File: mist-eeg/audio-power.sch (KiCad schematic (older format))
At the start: 18 parts, among them U6 LT3042xMSE, U7 LT3042xMSE

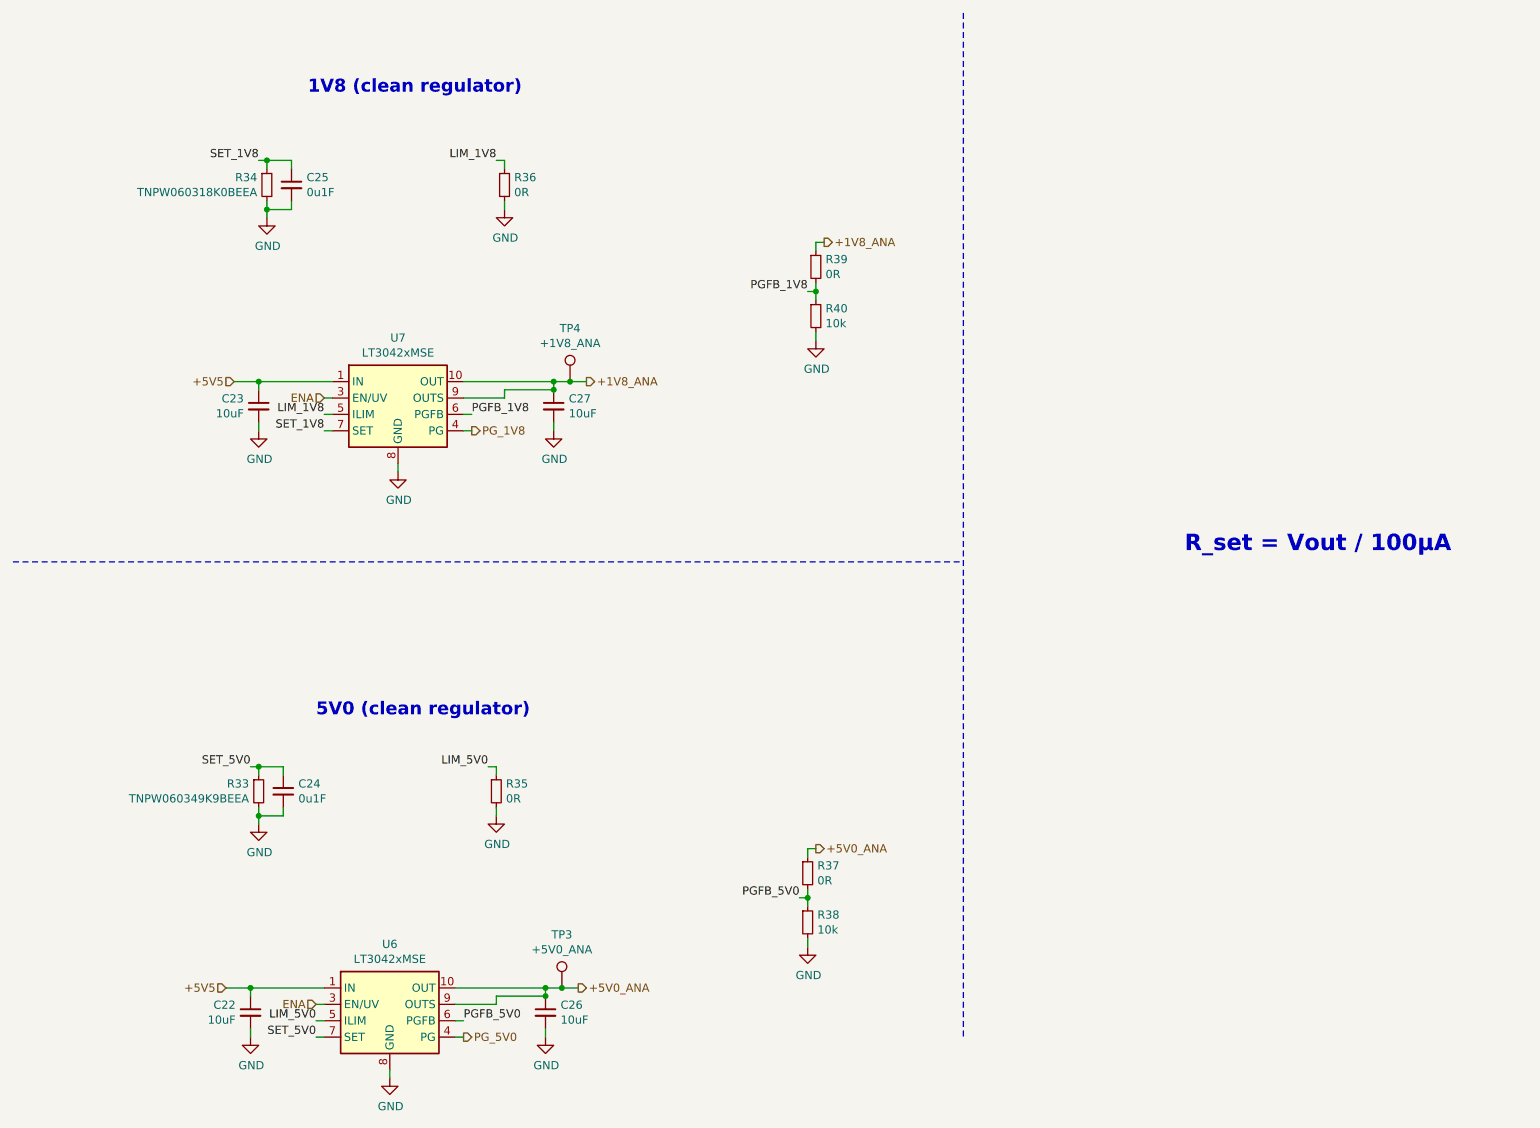
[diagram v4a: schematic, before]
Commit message: Change buckboost regulator used
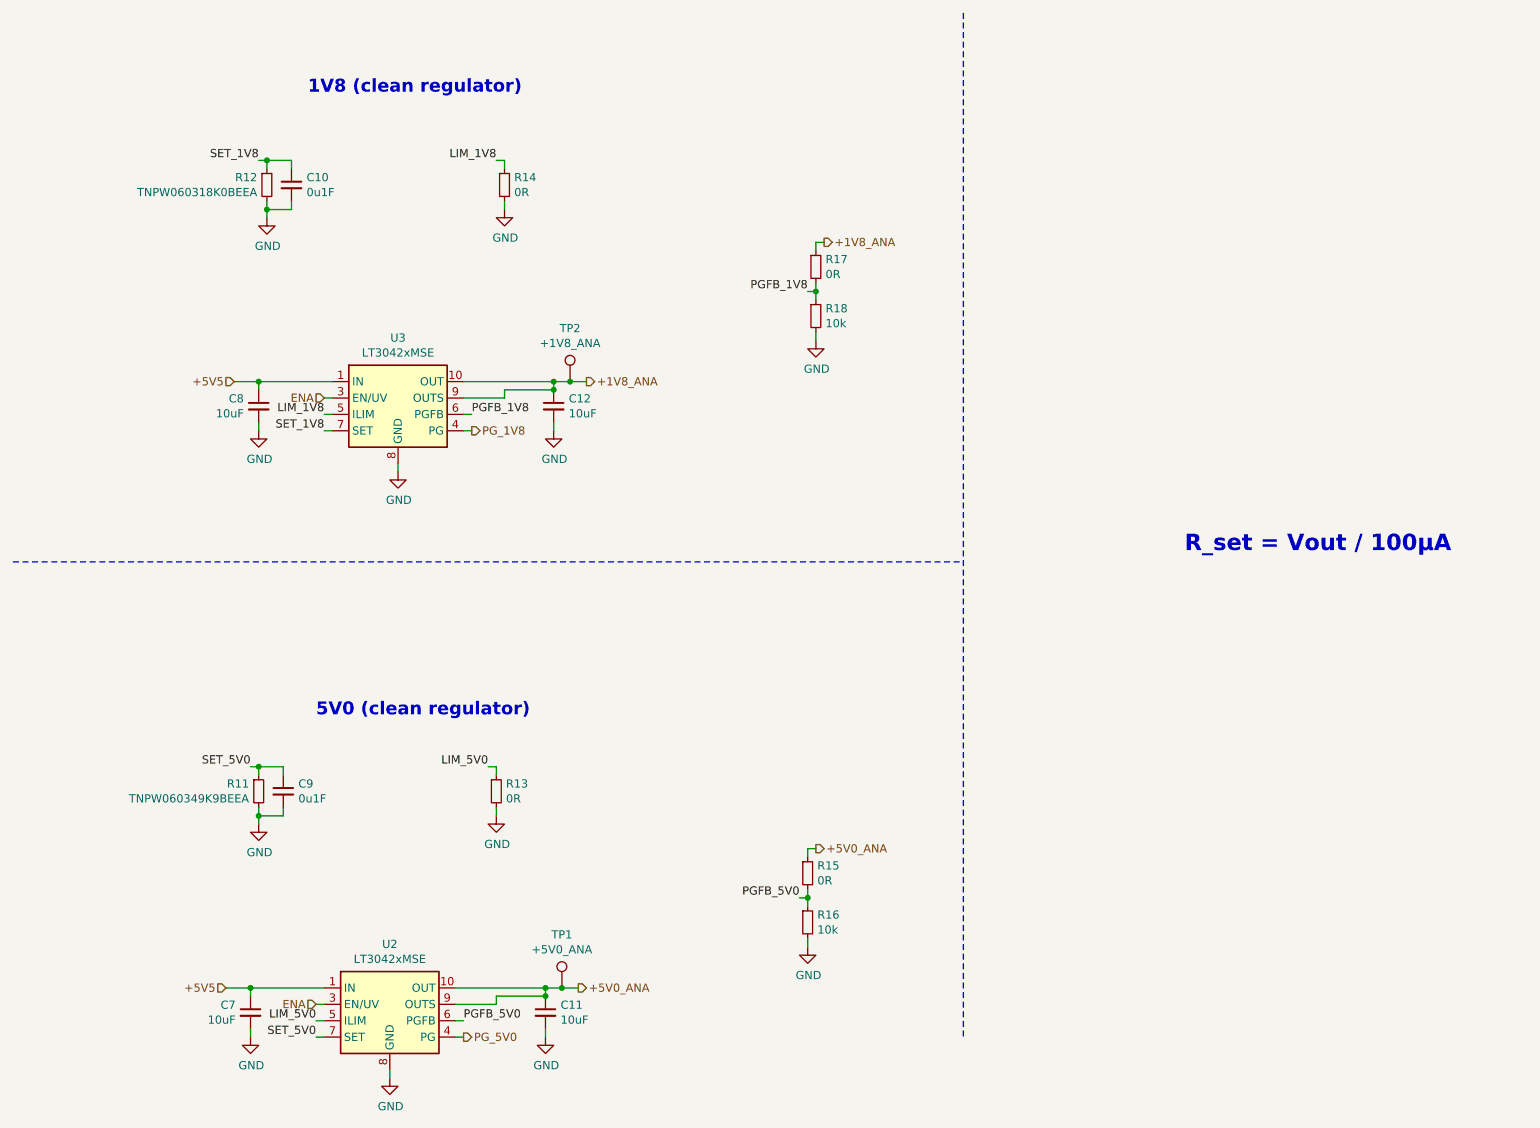
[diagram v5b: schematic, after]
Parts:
- renumbered C25 to C10, C26 to C11, C27 to C12, C22 to C7, C23 to C8, C24 to C9, R33 to R11, R34 to R12, R35 to R13, R36 to R14, R37 to R15, R38 to R16, R39 to R17, R40 to R18, TP3 to TP1, TP4 to TP2, U6 to U2, U7 to U3
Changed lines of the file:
@@
 Sheet 4 11
 Title "Portiloop"
-Date "2021-06-07"
-Rev "1A"
+Date "2021-08-03"
+Rev "1D"
 Comp "MIST Lab"
 Comment1 "Designed by Xavier L'Heureux"
@@
 $EndDescr
 $Comp
-L Regulator_Linear:LT3042xMSE U7
+L Regulator_Linear:LT3042xMSE U3
 U 1 1 60CC3292
 P 2850 2850
-F 0 "U7" H 2850 3217 50  0000 C CNN
+F 0 "U3" H 2850 3217 50  0000 C CNN
 F 1 "LT3042xMSE" H 2850 3126 50  0000 C CNN
 F 2 "Package_SO:MSOP-10-1EP_3x3mm_P0.5mm_EP1.68x1.88mm" H 2850 3175 50  0001 C CNN
@@
 +5V0_ANA
 $Comp
-L Device:C_Small C23
+L Device:C_Small C8
 U 1 1 60CDC893
 P 2000 2900
-F 0 "C23" H 1909 2946 50  0000 R CNN
+F 0 "C8" H 1909 2946 50  0000 R CNN
 F 1 "10uF" H 1909 2855 50  0000 R CNN
 F 2 "Capacitor_SMD:C_0603_1608Metric" H 2000 2900 50  0001 C CNN
@@
 	2000 3000 2000 3050
 $Comp
-L Device:C_Small C27
+L Device:C_Small C12
 U 1 1 60CE9660
 P 3800 2900
-F 0 "C27" H 3892 2946 50  0000 L CNN
+F 0 "C12" H 3892 2946 50  0000 L CNN
 F 1 "10uF" H 3892 2855 50  0000 L CNN
 F 2 "Capacitor_SMD:C_0603_1608Metric" H 3800 2900 50  0001 C CNN
@@
 	2400 2950 2450 2950
 $Comp
-L Device:R_Small R36
+L Device:R_Small R14
 U 1 1 60CFCD89
 P 3500 1550
-F 0 "R36" H 3559 1596 50  0000 L CNN
+F 0 "R14" H 3559 1596 50  0000 L CNN
 F 1 "0R" H 3559 1505 50  0000 L CNN
 F 2 "Resistor_SMD:R_0603_1608Metric" H 3500 1550 50  0001 C CNN
@@
 $EndComp
 $Comp
-L Device:R_Small R39
+L Device:R_Small R17
 U 1 1 60D00084
 P 5400 2050
-F 0 "R39" H 5459 2096 50  0000 L CNN
+F 0 "R17" H 5459 2096 50  0000 L CNN
 F 1 "0R" H 5459 2005 50  0000 L CNN
 F 2 "Resistor_SMD:R_0603_1608Metric" H 5400 2050 50  0001 C CNN
@@
 $EndComp
 $Comp
-L Device:R_Small R40
+L Device:R_Small R18
 U 1 1 60D0018E
 P 5400 2350
-F 0 "R40" H 5459 2396 50  0000 L CNN
+F 0 "R18" H 5459 2396 50  0000 L CNN
 F 1 "10k" H 5459 2305 50  0000 L CNN
 F 2 "Resistor_SMD:R_0603_1608Metric" H 5400 2350 50  0001 C CNN
@@
 	3500 1700 3500 1650
 $Comp
-L Device:R_Small R34
+L Device:R_Small R12
 U 1 1 60D04DA7
 P 2050 1550
-F 0 "R34" H 1991 1596 50  0000 R CNN
+F 0 "R12" H 1991 1596 50  0000 R CNN
 F 1 "TNPW060318K0BEEA" H 1991 1505 50  0000 R CNN
 F 2 "Resistor_SMD:R_0603_1608Metric" H 2050 1550 50  0001 C CNN
@@
 	5400 2200 5400 2250
 $Comp
-L Device:C_Small C25
+L Device:C_Small C10
 U 1 1 60D11AAE
 P 2200 1550
-F 0 "C25" H 2292 1596 50  0000 L CNN
+F 0 "C10" H 2292 1596 50  0000 L CNN
 F 1 "0u1F" H 2292 1505 50  0000 L CNN
 F 2 "Capacitor_SMD:C_0201_0603Metric" H 2200 1550 50  0001 C CNN
@@
 R_set = Vout / 100μA
 $Comp
-L Regulator_Linear:LT3042xMSE U6
+L Regulator_Linear:LT3042xMSE U2
 U 1 1 60D644F1
 P 2800 6550
-F 0 "U6" H 2800 6917 50  0000 C CNN
+F 0 "U2" H 2800 6917 50  0000 C CNN
 F 1 "LT3042xMSE" H 2800 6826 50  0000 C CNN
 F 2 "Package_SO:MSOP-10-1EP_3x3mm_P0.5mm_EP1.68x1.88mm" H 2800 6875 50  0001 C CNN
@@
 +5V0_ANA
 $Comp
-L Device:C_Small C22
+L Device:C_Small C7
 U 1 1 60D644F9
 P 1950 6600
-F 0 "C22" H 1859 6646 50  0000 R CNN
+F 0 "C7" H 1859 6646 50  0000 R CNN
 F 1 "10uF" H 1859 6555 50  0000 R CNN
 F 2 "Capacitor_SMD:C_0603_1608Metric" H 1950 6600 50  0001 C CNN
@@
 	1950 6700 1950 6750
 $Comp
-L Device:C_Small C26
+L Device:C_Small C11
 U 1 1 60D6450F
 P 3750 6600
-F 0 "C26" H 3842 6646 50  0000 L CNN
+F 0 "C11" H 3842 6646 50  0000 L CNN
 F 1 "10uF" H 3842 6555 50  0000 L CNN
 F 2 "Capacitor_SMD:C_0603_1608Metric" H 3750 6600 50  0001 C CNN
@@
 	2350 6650 2400 6650
 $Comp
-L Device:R_Small R35
+L Device:R_Small R13
 U 1 1 60D64530
 P 3450 5250
-F 0 "R35" H 3509 5296 50  0000 L CNN
+F 0 "R13" H 3509 5296 50  0000 L CNN
 F 1 "0R" H 3509 5205 50  0000 L CNN
 F 2 "Resistor_SMD:R_0603_1608Metric" H 3450 5250 50  0001 C CNN
@@
 $EndComp
 $Comp
-L Device:R_Small R37
+L Device:R_Small R15
 U 1 1 60D64536
 P 5350 5750
-F 0 "R37" H 5409 5796 50  0000 L CNN
+F 0 "R15" H 5409 5796 50  0000 L CNN
 F 1 "0R" H 5409 5705 50  0000 L CNN
 F 2 "Resistor_SMD:R_0603_1608Metric" H 5350 5750 50  0001 C CNN
@@
 $EndComp
 $Comp
-L Device:R_Small R38
+L Device:R_Small R16
 U 1 1 60D6453C
 P 5350 6050
-F 0 "R38" H 5409 6096 50  0000 L CNN
+F 0 "R16" H 5409 6096 50  0000 L CNN
 F 1 "10k" H 5409 6005 50  0000 L CNN
 F 2 "Resistor_SMD:R_0603_1608Metric" H 5350 6050 50  0001 C CNN
@@
 	3450 5400 3450 5350
 $Comp
-L Device:R_Small R33
+L Device:R_Small R11
 U 1 1 60D6454C
 P 2000 5250
-F 0 "R33" H 1941 5296 50  0000 R CNN
+F 0 "R11" H 1941 5296 50  0000 R CNN
 F 1 "TNPW060349K9BEEA" H 1941 5205 50  0000 R CNN
 F 2 "Resistor_SMD:R_0603_1608Metric" H 2000 5250 50  0001 C CNN
@@
 	5350 5900 5350 5950
 $Comp
-L Device:C_Small C24
+L Device:C_Small C9
 U 1 1 60D64568
 P 2150 5250
-F 0 "C24" H 2242 5296 50  0000 L CNN
+F 0 "C9" H 2242 5296 50  0000 L CNN
 F 1 "0u1F" H 2242 5205 50  0000 L CNN
 F 2 "Capacitor_SMD:C_0201_0603Metric" H 2150 5250 50  0001 C CNN
@@
 5V0 (clean regulator)
 $Comp
-L Connector:TestPoint TP4
+L Connector:TestPoint TP2
 U 1 1 60C25634
 P 3900 2750
-F 0 "TP4" H 3900 3075 50  0000 C CNN
+F 0 "TP2" H 3900 3075 50  0000 C CNN
 F 1 "+1V8_ANA" H 3900 2984 50  0000 C CNN
 F 2 "TestPoint:TestPoint_Pad_D1.0mm" H 4100 2750 50  0001 C CNN
@@
 Connection ~ 3900 2750
 $Comp
-L Connector:TestPoint TP3
+L Connector:TestPoint TP1
 U 1 1 60C2D0B0
 P 3850 6450
-F 0 "TP3" H 3850 6775 50  0000 C CNN
+F 0 "TP1" H 3850 6775 50  0000 C CNN
 F 1 "+5V0_ANA" H 3850 6684 50  0000 C CNN
 F 2 "TestPoint:TestPoint_Pad_D1.0mm" H 4050 6450 50  0001 C CNN
@@
 ENA
 $Comp
-L power:GND #PWR051
+L power:GND #PWR023
 U 1 1 610B067C
 P 3800 3050
-F 0 "#PWR051" H 3800 2800 50  0001 C CNN
+F 0 "#PWR023" H 3800 2800 50  0001 C CNN
 F 1 "GND" H 3805 2877 50  0000 C CNN
 F 2 "" H 3800 3050 50  0001 C CNN
@@
 $EndComp
 $Comp
-L power:GND #PWR047
+L power:GND #PWR019
 U 1 1 610B0AB0
 P 2850 3300
-F 0 "#PWR047" H 2850 3050 50  0001 C CNN
+F 0 "#PWR019" H 2850 3050 50  0001 C CNN
 F 1 "GND" H 2855 3127 50  0000 C CNN
 F 2 "" H 2850 3300 50  0001 C CNN
@@
 $EndComp
 $Comp
-L power:GND #PWR043
+L power:GND #PWR015
 U 1 1 610B0EE6
 P 2000 3050
-F 0 "#PWR043" H 2000 2800 50  0001 C CNN
+F 0 "#PWR015" H 2000 2800 50  0001 C CNN
 F 1 "GND" H 2005 2877 50  0000 C CNN
 F 2 "" H 2000 3050 50  0001 C CNN
@@
 $EndComp
 $Comp
-L power:GND #PWR053
+L power:GND #PWR025
 U 1 1 610B1308
 P 5400 2500
-F 0 "#PWR053" H 5400 2250 50  0001 C CNN
+F 0 "#PWR025" H 5400 2250 50  0001 C CNN
 F 1 "GND" H 5405 2327 50  0000 C CNN
 F 2 "" H 5400 2500 50  0001 C CNN
@@
 $EndComp
 $Comp
-L power:GND #PWR049
+L power:GND #PWR021
 U 1 1 610B1758
 P 3500 1700
-F 0 "#PWR049" H 3500 1450 50  0001 C CNN
+F 0 "#PWR021" H 3500 1450 50  0001 C CNN
 F 1 "GND" H 3505 1527 50  0000 C CNN
 F 2 "" H 3500 1700 50  0001 C CNN
@@
 $EndComp
 $Comp
-L power:GND #PWR045
+L power:GND #PWR017
 U 1 1 610B1BAA
 P 2050 1750
-F 0 "#PWR045" H 2050 1500 50  0001 C CNN
+F 0 "#PWR017" H 2050 1500 50  0001 C CNN
 F 1 "GND" H 2055 1577 50  0000 C CNN
 F 2 "" H 2050 1750 50  0001 C CNN
@@
 $EndComp
 $Comp
-L power:GND #PWR044
+L power:GND #PWR016
 U 1 1 610B1FD2
 P 2000 5450
-F 0 "#PWR044" H 2000 5200 50  0001 C CNN
+F 0 "#PWR016" H 2000 5200 50  0001 C CNN
 F 1 "GND" H 2005 5277 50  0000 C CNN
 F 2 "" H 2000 5450 50  0001 C CNN
@@
 $EndComp
 $Comp
-L power:GND #PWR048
+L power:GND #PWR020
 U 1 1 610B2412
 P 3450 5400
-F 0 "#PWR048" H 3450 5150 50  0001 C CNN
+F 0 "#PWR020" H 3450 5150 50  0001 C CNN
 F 1 "GND" H 3455 5227 50  0000 C CNN
 F 2 "" H 3450 5400 50  0001 C CNN
@@
 $EndComp
 $Comp
-L power:GND #PWR052
+L power:GND #PWR024
 U 1 1 610B2854
 P 5350 6200
-F 0 "#PWR052" H 5350 5950 50  0001 C CNN
+F 0 "#PWR024" H 5350 5950 50  0001 C CNN
 F 1 "GND" H 5355 6027 50  0000 C CNN
 F 2 "" H 5350 6200 50  0001 C CNN
@@
 $EndComp
 $Comp
-L power:GND #PWR050
+L power:GND #PWR022
 U 1 1 610B2C71
 P 3750 6750
-F 0 "#PWR050" H 3750 6500 50  0001 C CNN
+F 0 "#PWR022" H 3750 6500 50  0001 C CNN
 F 1 "GND" H 3755 6577 50  0000 C CNN
 F 2 "" H 3750 6750 50  0001 C CNN
@@
 $EndComp
 $Comp
-L power:GND #PWR046
+L power:GND #PWR018
 U 1 1 610B30B7
 P 2800 7000
-F 0 "#PWR046" H 2800 6750 50  0001 C CNN
+F 0 "#PWR018" H 2800 6750 50  0001 C CNN
 F 1 "GND" H 2805 6827 50  0000 C CNN
 F 2 "" H 2800 7000 50  0001 C CNN
@@
 $EndComp
 $Comp
-L power:GND #PWR042
+L power:GND #PWR014
 U 1 1 610B34FF
 P 1950 6750
-F 0 "#PWR042" H 1950 6500 50  0001 C CNN
+F 0 "#PWR014" H 1950 6500 50  0001 C CNN
 F 1 "GND" H 1955 6577 50  0000 C CNN
 F 2 "" H 1950 6750 50  0001 C CNN
